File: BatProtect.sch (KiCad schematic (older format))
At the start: 22 parts, among them J1 Bat, J2 Load, Q1 Q_PMOS_GDS, Q2 SI2308, SW1 SW_DIP_x01, U1 ATTINY13A-SU, U2 MIC5235-5.0

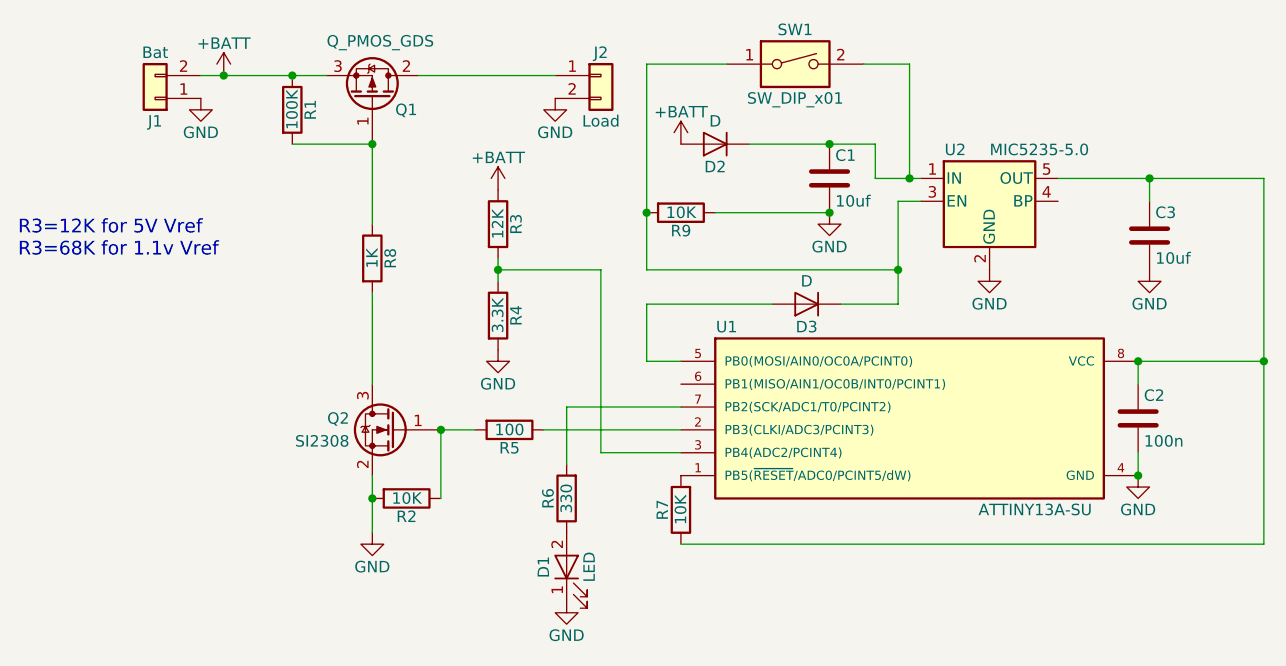
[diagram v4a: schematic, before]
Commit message: Changed the mosfet to better one. PCB redesign
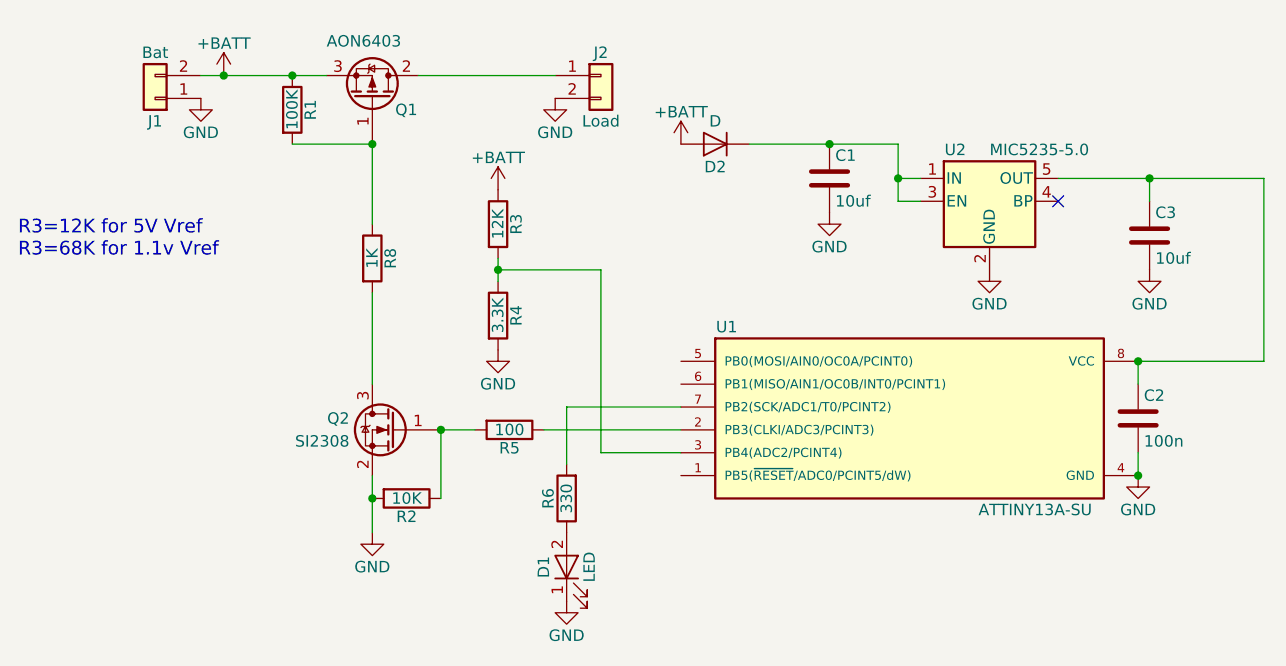
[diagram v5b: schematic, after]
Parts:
- removed D3: D, Diodes_SMD:D_SOD-323_HandSoldering, symbol D
- removed R7, R9: 10K, Resistors_SMD:R_0603_HandSoldering, symbol R
- removed SW1: SW_DIP_x01, Buttons_Switches_THT:SW_PUSH_6mm, symbol SW_DIP_x01
- C1, C2, C3: footprint Capacitors_SMD:C_0603_HandSoldering -> Capacitors_SMD:C_0603
- D1: footprint LEDs:LED_0805_HandSoldering -> LEDs:LED_0805
- J1, J2: footprint KiCad_custom:Conn2pin_2.54mm -> KiCadCustomLibs:Connector_2x5mm_1.5Drill
- Q1: value Q_PMOS_GDS -> AON6403; footprint TO_SOT_Packages_SMD:TO-263-2 -> KiCadCustomLibs:DFN-8-1EP_6x5mm
- R1, R2, R3, R4, R5, R6, R8: footprint Resistors_SMD:R_0603_HandSoldering -> Resistors_SMD:R_0603
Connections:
- net at C1.1, D2.1 (K), U2.1 (IN): now also U2.3 (EN)
- no-connect marks 0 -> 1
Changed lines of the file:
@@
 F 0 "J1" H 4300 2150 50  0000 C CNN
 F 1 "Bat" H 4300 1850 50  0000 C CNN
-F 2 "KiCad_custom:Conn2pin_2.54mm" H 4300 2050 50  0001 C CNN
+F 2 "KiCadCustomLibs:Connector_2x5mm_1.5Drill" H 4300 2050 50  0001 C CNN
 F 3 "" H 4300 2050 50  0001 C CNN
 	1    4300 2050
@@
 F 0 "J2" H 6250 2050 50  0000 C CNN
 F 1 "Load" H 6250 1750 50  0000 C CNN
-F 2 "KiCad_custom:Conn2pin_2.54mm" H 6250 1950 50  0001 C CNN
+F 2 "KiCadCustomLibs:Connector_2x5mm_1.5Drill" H 6250 1950 50  0001 C CNN
 F 3 "" H 6250 1950 50  0001 C CNN
 	1    6250 1950
@@
 $EndComp
 $Comp
-L GND #PWR1
+L GND #PWR01
 U 1 1 59C3AFEF
 P 4500 2050
-F 0 "#PWR1" H 4500 1800 50  0001 C CNN
+F 0 "#PWR01" H 4500 1800 50  0001 C CNN
 F 1 "GND" H 4500 1900 50  0000 C CNN
 F 2 "" H 4500 2050 50  0001 C CNN
@@
 $EndComp
 $Comp
-L GND #PWR6
+L GND #PWR02
 U 1 1 59C3B00A
 P 6050 2050
-F 0 "#PWR6" H 6050 1800 50  0001 C CNN
+F 0 "#PWR02" H 6050 1800 50  0001 C CNN
 F 1 "GND" H 6050 1900 50  0000 C CNN
 F 2 "" H 6050 2050 50  0001 C CNN
@@
 $EndComp
 $Comp
-L GND #PWR3
+L GND #PWR03
 U 1 1 59C3B119
 P 5250 3950
-F 0 "#PWR3" H 5250 3700 50  0001 C CNN
+F 0 "#PWR03" H 5250 3700 50  0001 C CNN
 F 1 "GND" H 5250 3800 50  0000 C CNN
 F 2 "" H 5250 3950 50  0001 C CNN
@@
 F 0 "R1" V 4980 2100 50  0000 C CNN
 F 1 "100K" V 4900 2100 50  0000 C CNN
-F 2 "Resistors_SMD:R_0603_HandSoldering" V 4830 2100 50  0001 C CNN
+F 2 "Resistors_SMD:R_0603" V 4830 2100 50  0001 C CNN
 F 3 "" H 4900 2100 50  0001 C CNN
 	1    4900 2100
@@
 F 0 "R2" V 5480 3800 50  0000 C CNN
 F 1 "10K" V 5400 3800 50  0000 C CNN
-F 2 "Resistors_SMD:R_0603_HandSoldering" V 5330 3800 50  0001 C CNN
+F 2 "Resistors_SMD:R_0603" V 5330 3800 50  0001 C CNN
 F 3 "" H 5400 3800 50  0001 C CNN
 	1    5400 3800
@@
 F 0 "R5" V 5930 3500 50  0000 C CNN
 F 1 "100" V 5850 3500 50  0000 C CNN
-F 2 "Resistors_SMD:R_0603_HandSoldering" V 5780 3500 50  0001 C CNN
+F 2 "Resistors_SMD:R_0603" V 5780 3500 50  0001 C CNN
 F 3 "" H 5850 3500 50  0001 C CNN
 	1    5850 3500
@@
 $EndComp
 $Comp
-L +BATT #PWR2
+L +BATT #PWR04
 U 1 1 59C3BDD2
 P 4600 1950
-F 0 "#PWR2" H 4600 1800 50  0001 C CNN
+F 0 "#PWR04" H 4600 1800 50  0001 C CNN
 F 1 "+BATT" H 4600 2090 50  0000 C CNN
 F 2 "" H 4600 1950 50  0001 C CNN
@@
 F 0 "R3" V 5880 2600 50  0000 C CNN
 F 1 "12K" V 5800 2600 50  0000 C CNN
-F 2 "Resistors_SMD:R_0603_HandSoldering" V 5730 2600 50  0001 C CNN
+F 2 "Resistors_SMD:R_0603" V 5730 2600 50  0001 C CNN
 F 3 "" H 5800 2600 50  0001 C CNN
 	1    5800 2600
@@
 F 0 "R4" V 5880 3000 50  0000 C CNN
 F 1 "3.3K" V 5800 3000 50  0000 C CNN
-F 2 "Resistors_SMD:R_0603_HandSoldering" V 5730 3000 50  0001 C CNN
+F 2 "Resistors_SMD:R_0603" V 5730 3000 50  0001 C CNN
 F 3 "" H 5800 3000 50  0001 C CNN
 	1    5800 3000
@@
 $EndComp
 $Comp
-L GND #PWR5
+L GND #PWR05
 U 1 1 59C3C352
 P 5800 3150
-F 0 "#PWR5" H 5800 2900 50  0001 C CNN
+F 0 "#PWR05" H 5800 2900 50  0001 C CNN
 F 1 "GND" H 5800 3000 50  0000 C CNN
 F 2 "" H 5800 3150 50  0001 C CNN
@@
 $EndComp
 $Comp
-L +BATT #PWR4
+L +BATT #PWR06
 U 1 1 59C3C431
 P 5800 2450
-F 0 "#PWR4" H 5800 2300 50  0001 C CNN
+F 0 "#PWR06" H 5800 2300 50  0001 C CNN
 F 1 "+BATT" H 5800 2590 50  0000 C CNN
 F 2 "" H 5800 2450 50  0001 C CNN
@@
 $EndComp
 $Comp
-L GND #PWR10
+L GND #PWR07
 U 1 1 59C3C847
 P 7950 2800
-F 0 "#PWR10" H 7950 2550 50  0001 C CNN
+F 0 "#PWR07" H 7950 2550 50  0001 C CNN
 F 1 "GND" H 7950 2650 50  0000 C CNN
 F 2 "" H 7950 2800 50  0001 C CNN
@@
 $EndComp
 $Comp
-L GND #PWR11
+L GND #PWR08
 U 1 1 59C3C889
 P 8600 3700
-F 0 "#PWR11" H 8600 3450 50  0001 C CNN
+F 0 "#PWR08" H 8600 3450 50  0001 C CNN
 F 1 "GND" H 8600 3550 50  0000 C CNN
 F 2 "" H 8600 3700 50  0001 C CNN
@@
 $EndComp
 $Comp
-L +BATT #PWR8
+L +BATT #PWR09
 U 1 1 59C3CB6E
 P 6600 2250
-F 0 "#PWR8" H 6600 2100 50  0001 C CNN
+F 0 "#PWR09" H 6600 2100 50  0001 C CNN
 F 1 "+BATT" H 6600 2390 50  0000 C CNN
 F 2 "" H 6600 2250 50  0001 C CNN
@@
 	1    0    0    -1
 $EndComp
-$Comp
-L D D3
-U 1 1 59C3D1B2
-P 7150 2950
-F 0 "D3" H 7150 3050 50  0000 C CNN
-F 1 "D" H 7150 2850 50  0000 C CNN
-F 2 "Diodes_SMD:D_SOD-323_HandSoldering" H 7150 2950 50  0001 C CNN
-F 3 "" H 7150 2950 50  0001 C CNN
-	1    7150 2950
-	-1   0    0    1
-$EndComp
-$Comp
-L SW_DIP_x01 SW1
-U 1 1 59C3D3AC
-P 7100 1900
-F 0 "SW1" H 7100 2050 50  0000 C CNN
-F 1 "SW_DIP_x01" H 7100 1750 50  0000 C CNN
-F 2 "Buttons_Switches_THT:SW_PUSH_6mm" H 7100 1900 50  0001 C CNN
-F 3 "" H 7100 1900 50  0001 C CNN
-	1    7100 1900
-	1    0    0    -1
-$EndComp
 Wire Wire Line
 	4500 1950 5050 1950
@@
 Connection ~ 5800 2800
 Wire Wire Line
-	6900 2250 7450 2250
-Wire Wire Line
-	7450 2400 7650 2400
-Wire Wire Line
-	7650 2500 7550 2500
-Wire Wire Line
-	7550 2500 7550 2950
-Wire Wire Line
-	6450 3200 6600 3200
-Wire Wire Line
-	7400 1900 7600 1900
-Wire Wire Line
-	7600 1900 7600 2400
-Connection ~ 7600 2400
-Wire Wire Line
-	7550 2800 6450 2800
-Wire Wire Line
-	6450 2800 6450 1900
-Wire Wire Line
-	6450 1900 6800 1900
-Connection ~ 7550 2800
+	6900 2250 7550 2250
+Wire Wire Line
+	7550 2400 7650 2400
+Wire Wire Line
+	7550 2500 7650 2500
 $Comp
 L C C2
@@
 F 0 "C2" H 8625 3550 50  0000 L CNN
 F 1 "100n" H 8625 3350 50  0000 L CNN
-F 2 "Capacitors_SMD:C_0603_HandSoldering" H 8638 3300 50  0001 C CNN
+F 2 "Capacitors_SMD:C_0603" H 8638 3300 50  0001 C CNN
 F 3 "" H 8600 3450 50  0001 C CNN
 	1    8600 3450
@@
 F 0 "C3" H 8675 2750 50  0000 L CNN
 F 1 "10uf" H 8675 2550 50  0000 L CNN
-F 2 "Capacitors_SMD:C_0603_HandSoldering" H 8688 2500 50  0001 C CNN
+F 2 "Capacitors_SMD:C_0603" H 8688 2500 50  0001 C CNN
 F 3 "" H 8650 2650 50  0001 C CNN
 	1    8650 2650
@@
 	8650 2400 8650 2500
 $Comp
-L GND #PWR12
+L GND #PWR010
 U 1 1 59C3DC12
 P 8650 2800
-F 0 "#PWR12" H 8650 2550 50  0001 C CNN
+F 0 "#PWR010" H 8650 2550 50  0001 C CNN
 F 1 "GND" H 8650 2650 50  0000 C CNN
 F 2 "" H 8650 2800 50  0001 C CNN
@@
 Wire Wire Line
 	8600 3700 8600 3600
-Wire Wire Line
-	9150 2400 9150 4000
 Wire Wire Line
 	9150 3200 8600 3200
@@
 F 0 "D1" H 6100 4200 50  0000 C CNN
 F 1 "LED" H 6100 4000 50  0000 C CNN
-F 2 "LEDs:LED_0805_HandSoldering" H 6100 4100 50  0001 C CNN
+F 2 "LEDs:LED_0805" H 6100 4100 50  0001 C CNN
 F 3 "" H 6100 4100 50  0001 C CNN
 	1    6100 4100
@@
 $EndComp
 $Comp
-L GND #PWR7
+L GND #PWR011
 U 1 1 59C3E67B
 P 6100 4250
-F 0 "#PWR7" H 6100 4000 50  0001 C CNN
+F 0 "#PWR011" H 6100 4000 50  0001 C CNN
 F 1 "GND" H 6100 4100 50  0000 C CNN
 F 2 "" H 6100 4250 50  0001 C CNN
@@
 F 0 "R6" V 6180 3800 50  0000 C CNN
 F 1 "330" V 6100 3800 50  0000 C CNN
-F 2 "Resistors_SMD:R_0603_HandSoldering" V 6030 3800 50  0001 C CNN
+F 2 "Resistors_SMD:R_0603" V 6030 3800 50  0001 C CNN
 F 3 "" H 6100 3800 50  0001 C CNN
 	1    6100 3800
@@
 Wire Wire Line
 	6100 3400 6600 3400
-$Comp
-L R R7
-U 1 1 59C3EB2B
-P 6600 3850
-F 0 "R7" V 6680 3850 50  0000 C CNN
-F 1 "10K" V 6600 3850 50  0000 C CNN
-F 2 "Resistors_SMD:R_0603_HandSoldering" V 6530 3850 50  0001 C CNN
-F 3 "" H 6600 3850 50  0001 C CNN
-	1    6600 3850
-	-1   0    0    1
-$EndComp
-Wire Wire Line
-	9150 4000 6600 4000
-Connection ~ 9150 3200
 Connection ~ 4900 1950
 $Comp
@@
 P 5250 2050
 F 0 "Q1" V 5200 2150 50  0000 L CNN
-F 1 "Q_PMOS_GDS" V 5500 1850 50  0000 L CNN
-F 2 "TO_SOT_Packages_SMD:TO-263-2" H 5450 2150 50  0001 C CNN
+F 1 "AON6403" V 5500 1850 50  0000 L CNN
+F 2 "KiCadCustomLibs:DFN-8-1EP_6x5mm" H 5450 2150 50  0001 C CNN
 F 3 "" H 5250 2050 50  0001 C CNN
 	1    5250 2050
@@
 F 0 "R8" V 5330 2750 50  0000 C CNN
 F 1 "1K" V 5250 2750 50  0000 C CNN
-F 2 "Resistors_SMD:R_0603_HandSoldering" V 5180 2750 50  0001 C CNN
+F 2 "Resistors_SMD:R_0603" V 5180 2750 50  0001 C CNN
 F 3 "" H 5250 2750 50  0001 C CNN
 	1    5250 2750
@@
 $EndComp
 Wire Wire Line
-	7450 2250 7450 2400
+	7550 2250 7550 2500
 $Comp
 L C C1
@@
 F 0 "C1" H 7275 2500 50  0000 L CNN
 F 1 "10uf" H 7275 2300 50  0000 L CNN
-F 2 "Capacitors_SMD:C_0603_HandSoldering" H 7288 2250 50  0001 C CNN
+F 2 "Capacitors_SMD:C_0603" H 7288 2250 50  0001 C CNN
 F 3 "" H 7250 2400 50  0001 C CNN
 	1    7250 2400
@@
 Connection ~ 7250 2250
 $Comp
-L GND #PWR9
+L GND #PWR012
 U 1 1 59F8B3C6
 P 7250 2550
-F 0 "#PWR9" H 7250 2300 50  0001 C CNN
+F 0 "#PWR012" H 7250 2300 50  0001 C CNN
 F 1 "GND" H 7250 2400 50  0000 C CNN
 F 2 "" H 7250 2550 50  0001 C CNN
@@
 	1    0    0    -1
 $EndComp
-Wire Wire Line
-	7550 2950 7300 2950
-Wire Wire Line
-	7000 2950 6450 2950
-Wire Wire Line
-	6450 2950 6450 3200
-$Comp
-L R R9
-U 1 1 59F8BC55
-P 6600 2550
-F 0 "R9" V 6680 2550 50  0000 C CNN
-F 1 "10K" V 6600 2550 50  0000 C CNN
-F 2 "Resistors_SMD:R_0603_HandSoldering" V 6530 2550 50  0001 C CNN
-F 3 "" H 6600 2550 50  0001 C CNN
-	1    6600 2550
-	0    1    1    0
-$EndComp
-Wire Wire Line
-	6750 2550 7250 2550
-Connection ~ 7250 2550
-Connection ~ 6450 2550
 Text Notes 3700 2750 0    60   ~ 0
 R3=12K for 5V Vref\nR3=68K for 1.1v Vref
+Connection ~ 7550 2400
+NoConn ~ 8250 2500
+Wire Wire Line
+	9150 2400 9150 3200
 $EndSCHEMATC

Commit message: Adjust resistor value to get safe Vgs
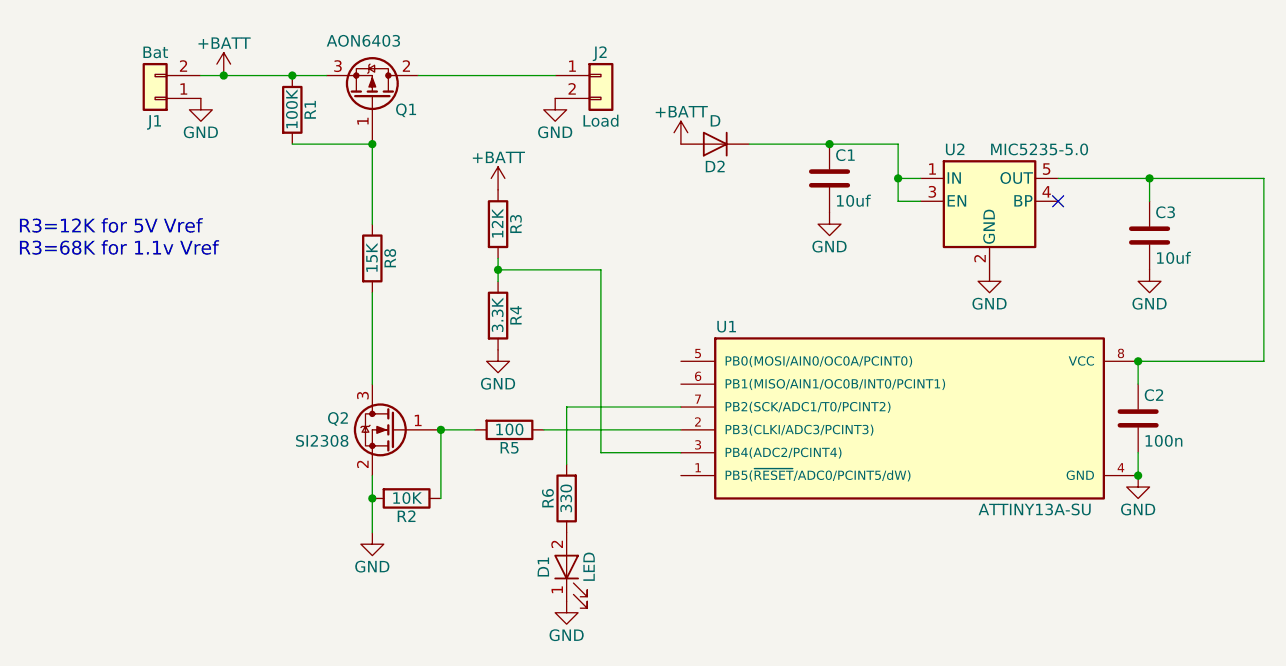
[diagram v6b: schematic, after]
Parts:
- R8: value 1K -> 15K
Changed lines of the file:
@@
 P 5250 2750
 F 0 "R8" V 5330 2750 50  0000 C CNN
-F 1 "1K" V 5250 2750 50  0000 C CNN
+F 1 "15K" V 5250 2750 50  0000 C CNN
 F 2 "Resistors_SMD:R_0603" V 5180 2750 50  0001 C CNN
 F 3 "" H 5250 2750 50  0001 C CNN
